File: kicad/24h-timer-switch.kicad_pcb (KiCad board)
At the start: 2 copper layers, 40.7 x 25.9 mm, 17 parts, among them J1 Barrel_Jack, J2 Screw_Terminal_01x02, Q1 FDS4559, SW1 SW_SPST, U1 AMS1117-5.0, U2 ATtiny85-20PU

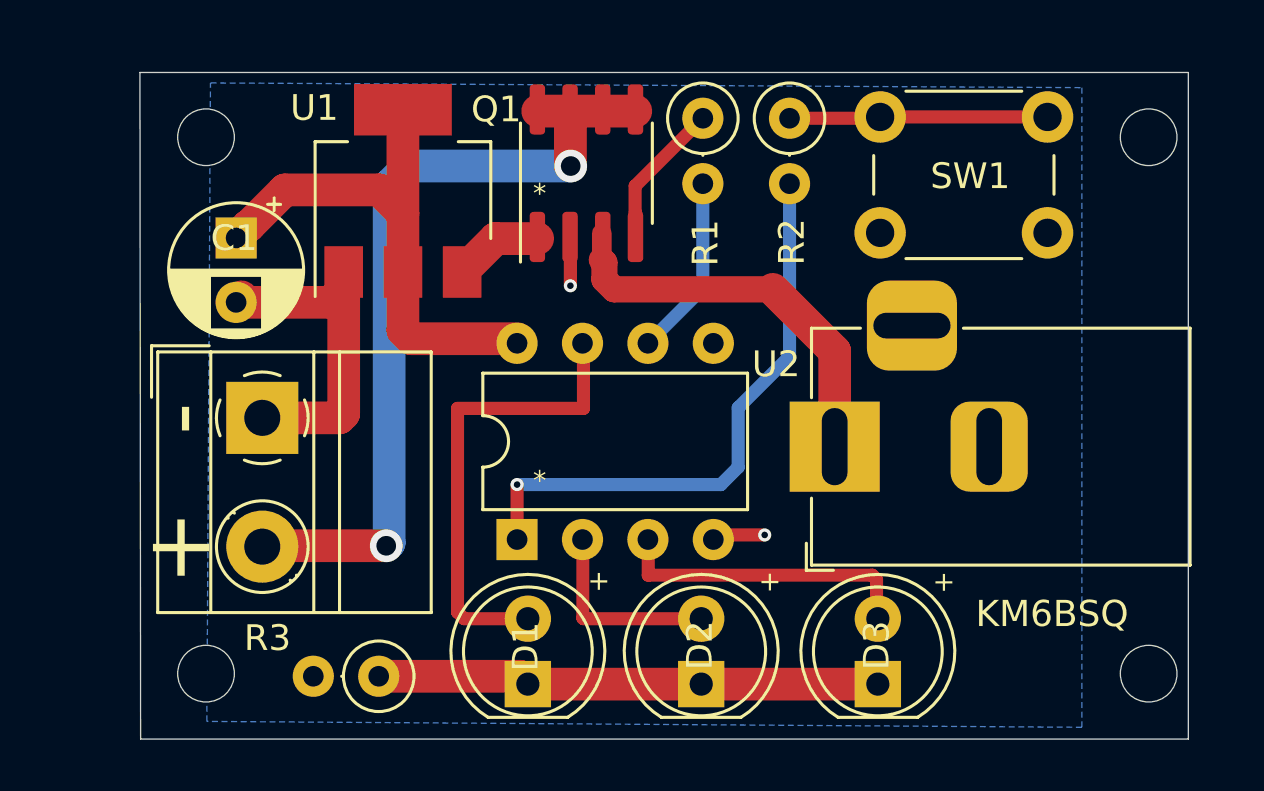
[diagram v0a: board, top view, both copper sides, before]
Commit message: add jumper selector
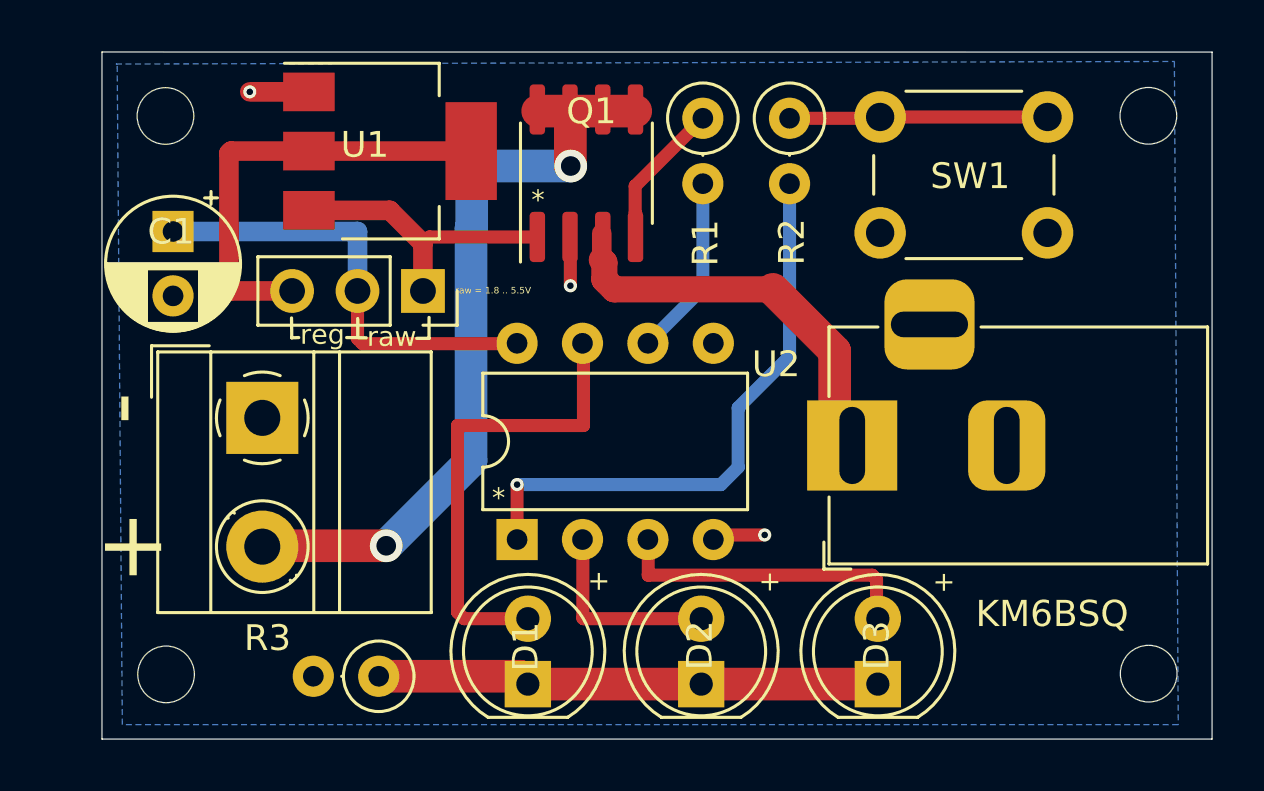
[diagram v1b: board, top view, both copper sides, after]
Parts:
- added J3: Conn_01x03, Connector_PinSocket_2.54mm:PinSocket_1x03_P2.54mm_Vertical, F.Cu at (126.5, 77.9)
- Q1: value FDS4559 -> AO4620
- moved C1 2.46 mm to (116.8, 75.5)
- moved REF** 1.78 mm to (116.5, 71.1)
- moved U1 1.62 mm to (125.3, 72.4), turned to 0 degrees
- moved REF** 1.55 mm to (116.6, 92.7)
- moved REF** 0.83 mm to (154.7, 71.0)
- moved J1 0.68 mm to (143.2, 83.8)
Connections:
- U1 pad 2: VCC -> V_OUT
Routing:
- net V_OUT: track 0.00 -> 17.2 mm
- net GND: track 18.6 -> 6.79 mm, vias 2 -> 3
- net V_IN: track 3.47 -> 11.4 mm
- net VCC: track 20.8 -> 17.6 mm
- net VDC: track 32.2 -> 30.6 mm
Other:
- board size 40.7 x 25.9 mm -> 43.1 x 26.7 mm
- board text added: "raw"
- board text added: "raw = 1.8 .. 5.5V"
- board text added: "reg"
